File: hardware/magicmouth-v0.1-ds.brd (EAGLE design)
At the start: 100 x 80 mm, 28 parts, among them IC1 LM386N, IC2 ATMEGA168-20P, J1 1X2-3.5MM, Q1 16Mhz, U1 ARDUINOR3-NOIOREF-NOTEXT, X1 STEREOJACK

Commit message: added 5V jumper to v0.1 single sided board
added 5V jumper to v0.1 single sided board

added 5V jumper to v0.1 single sided board

added 5V jumper to v0.1 single sided board

added 5V jumper to v0.1 single sided board
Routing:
- net GND: track 211.2 -> 158.2 mm
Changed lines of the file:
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@@
 <wire x1="63.935471875" y1="42.236525" x2="63.935471875" y2="42.345471875" width="0.4064" layer="16"/>
 <wire x1="63.935471875" y1="42.345471875" x2="66.675" y2="45.085" width="0.4064" layer="16"/>
-<wire x1="27.94" y1="15.24" x2="27.94" y2="12.7" width="0.254" layer="16"/>
-<wire x1="25.4" y1="15.24" x2="27.94" y2="15.24" width="0.254" layer="16"/>
-<wire x1="24.13" y1="16.51" x2="25.4" y2="15.24" width="0.254" layer="16"/>
+<wire x1="27.94" y1="15.24" x2="27.94" y2="12.7" width="0" layer="19" extent="1-16"/>
+<wire x1="25.4" y1="15.24" x2="27.94" y2="15.24" width="0" layer="19" extent="1-16"/>
+<wire x1="24.13" y1="16.51" x2="25.4" y2="15.24" width="0" layer="19" extent="1-16"/>
 <wire x1="27.94" y1="12.7" x2="27.432" y2="12.7" width="0.254" layer="16"/>
-<wire x1="38.1" y1="59.69" x2="36.83" y2="60.96" width="0.254" layer="1"/>
-<wire x1="62.23" y1="59.69" x2="38.1" y2="59.69" width="0.254" layer="1"/>
-<wire x1="62.23" y1="40.64" x2="62.23" y2="59.69" width="0.254" layer="1"/>
+<wire x1="38.1" y1="59.69" x2="36.83" y2="60.96" width="0" layer="19" extent="1-16"/>
+<wire x1="62.23" y1="59.69" x2="38.1" y2="59.69" width="0" layer="19" extent="1-16"/>
+<wire x1="62.23" y1="40.64" x2="62.23" y2="59.69" width="0" layer="19" extent="1-16"/>
 <wire x1="36.83" y1="60.96" x2="36.576" y2="60.96" width="0.254" layer="1"/>
-<wire x1="62.23" y1="40.64" x2="61.48605" y2="39.7871" width="0.254" layer="1"/>
+<wire x1="62.23" y1="40.64" x2="61.48605" y2="39.7871" width="0" layer="19" extent="1-16"/>
 <polygon width="0" layer="16" isolate="0.4064">
 <vertex x="10.16" y="10.16"/>

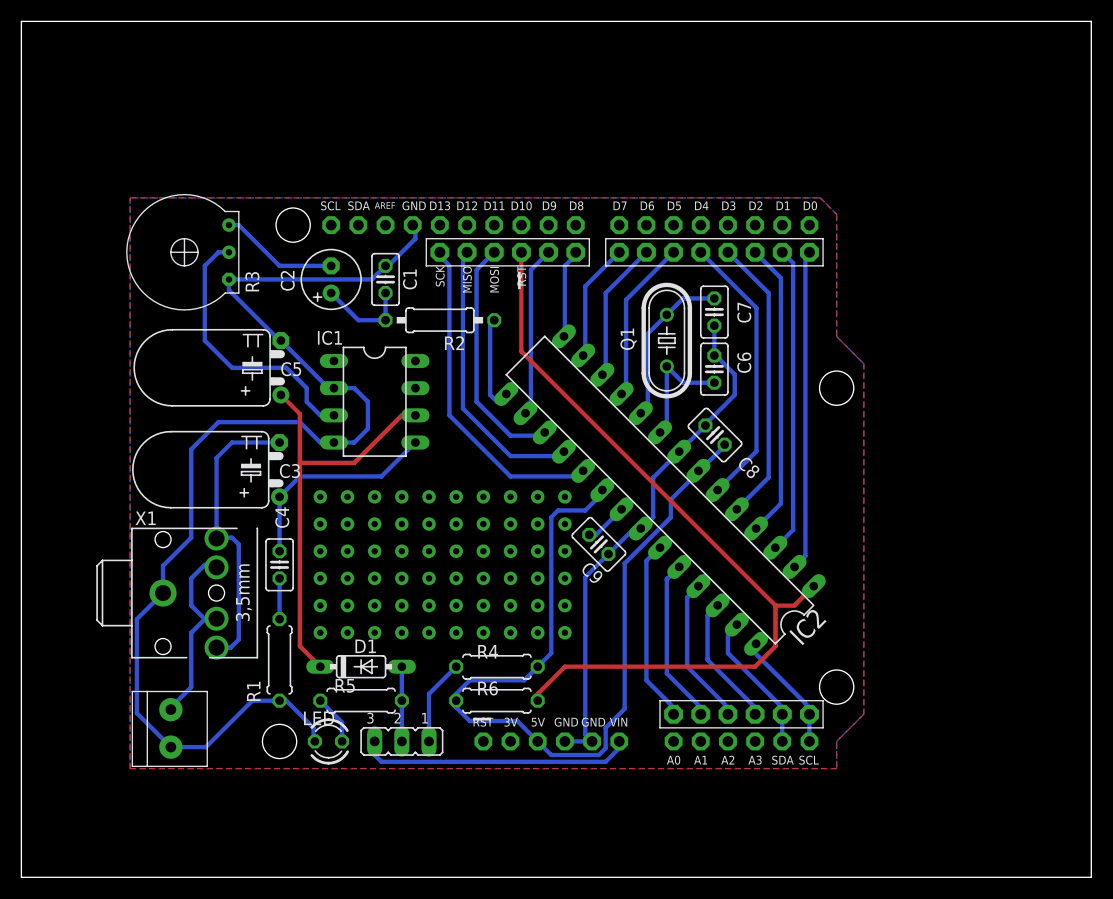
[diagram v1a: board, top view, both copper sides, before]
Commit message: added programming jumpers
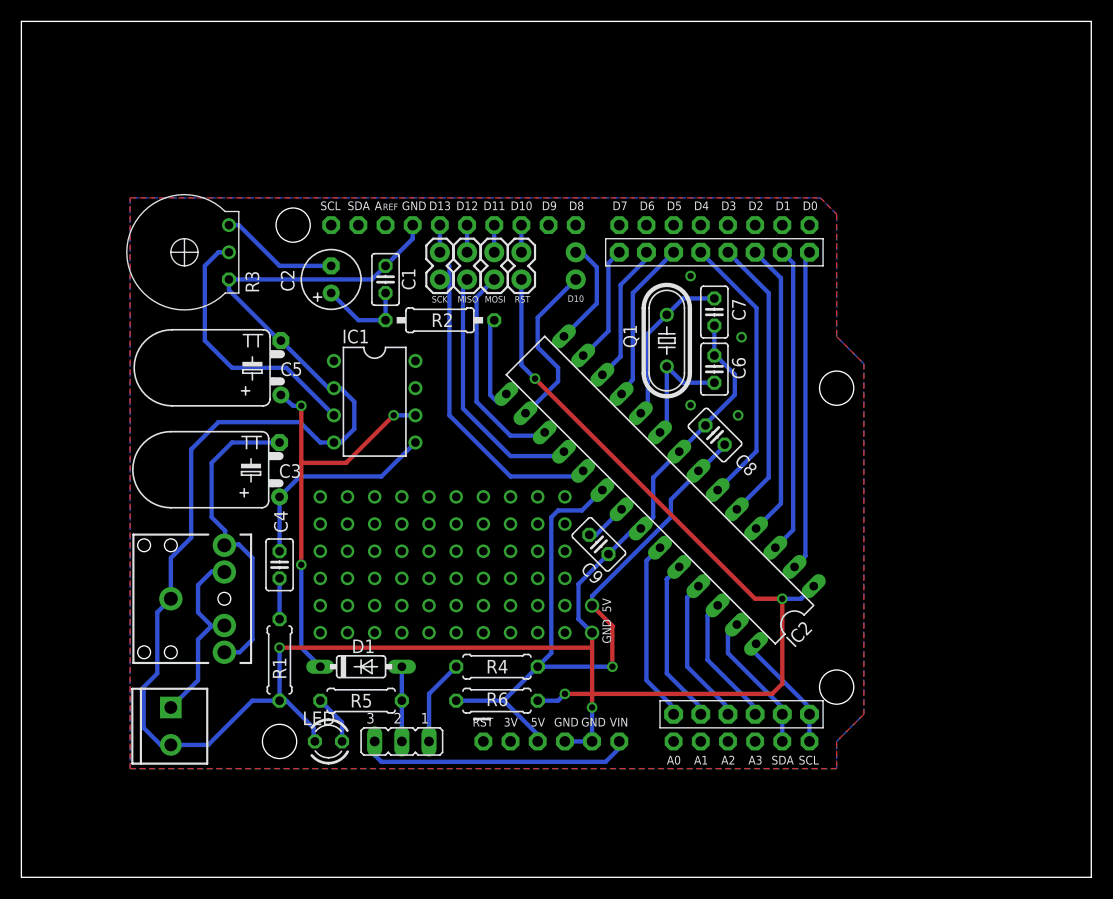
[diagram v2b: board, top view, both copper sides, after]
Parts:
- removed X1: STEREOJACK, adafruit:STX3100
- added JP5, JP6, JP7, JP8: (no value), SparkFun-Passives:1X02
- added U$2: AUDIO-JACK2PTH, SparkFun-Connectors:AUDIO-JACK
- J1: value 1X2-3.5MM -> (none); device adafruit:1X2-3.5MM -> SparkFun-Connectors:SCREWTERMINAL-3.5MM-2
- JP3: device adafruit:1X06-BIG -> SparkFun-Connectors:1X02_NO_SILK
- moved JP3 6.35 mm to (51.8, 58.4), turned to 270 degrees
- moved J1 1.90 mm to (14.0, 15.9)
- moved U$1 1.80 mm to (59.7, 22.2)
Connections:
- new net N$90: JP5.1, U1.D13
- new net N$91: JP6.1, U1.D12
- new net N$92: JP7.1, U1.D11
- new net N$93: JP8.1, U1.D10
- net +5V: now also IC2.7
- net GND: now also J1.2, U$2.SLEEVE; no longer J1.1, X1.1
- net MISO: now also JP6.2; no longer JP3.5
- net MOSI: now also JP7.2; no longer JP3.4
- net N$3: now also J1.1, U$2.RSH, U$2.TSH; no longer J1.2, X1.3, X1.4
- net N$8: now also U$2.RING, U$2.TIP; no longer X1.2, X1.5
- net SCK: now also JP5.2; no longer JP3.6
- net SS: now also JP8.2; no longer JP3.3
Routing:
- net GND: track 158.2 -> 189.0 mm, vias 0 -> 3
- net +5V: track 79.5 -> 68.0 mm, vias 0 -> 2
- net N$93: track 0.00 -> 2.54 mm
- net N$92: track 0.00 -> 2.54 mm
- net N$91: track 0.00 -> 2.54 mm
- net N$90: track 0.00 -> 2.54 mm
- net MOSI: track 22.5 -> 19.9 mm
- net MISO: track 26.2 -> 23.7 mm
- net N$24: track 8.31 -> 10.3 mm
- net SCK: track 30.7 -> 29.1 mm
- net N$8: track 27.7 -> 29.2 mm
- net N$9: track 25.5 -> 24.7 mm
- net SS: track 75.7 -> 76.3 mm, vias 0 -> 3
- net VS: track 39.6 -> 40.0 mm, vias 0 -> 3
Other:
- board text added: "A"
- board text added: "REF"
- board text removed: "AREF"

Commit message: reset switch on ss board; optional capacitor
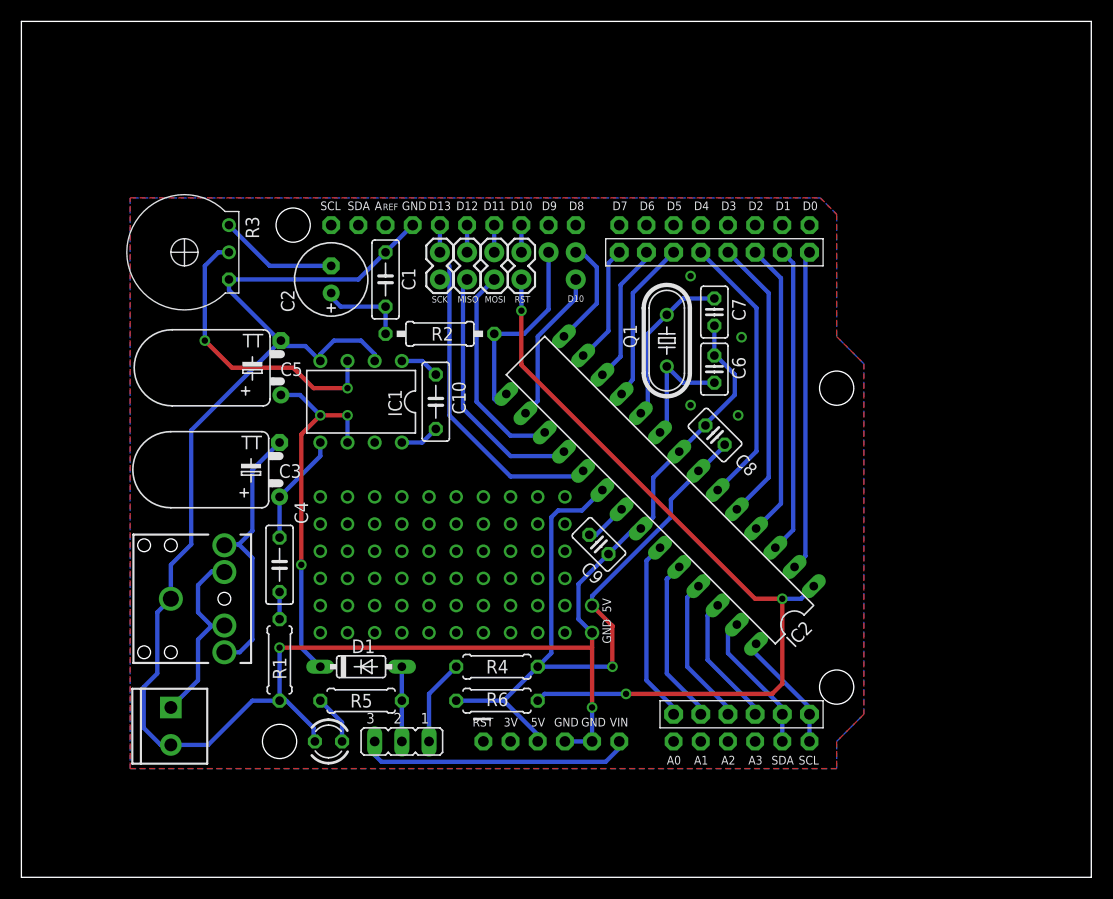
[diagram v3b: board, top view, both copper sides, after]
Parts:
- added C10: 1uF, rcl:C050-025X075
- added JP9: M01SMDNS, SparkFun-Connectors:1X01NS
- C1: device resistor:C025-025X050 -> rcl:C050-025X075
- C2: device resistor:E2,5-6 -> rcl:E2,5-7
- C4: device rcl:C025-025X050 -> rcl:C050-025X075
- moved IC1 1.27 mm to (31.8, 44.5), turned to 180 degrees
- moved R2 1.27 mm to (39.1, 50.8)
- moved U$1 0.63 mm to (59.7, 22.9)
- turned JP3 to 180 degrees
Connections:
- new net N$98: C10.1, IC1.1
- new net N$99: C10.2, IC1.8
- net N$12: now also JP9.1; no longer JP3.2
- net SIGNAL: now also JP3.2
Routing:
- net SIGNAL: track 9.21 -> 19.0 mm
- net N$1: track 19.9 -> 10.5 mm
- net VS: track 40.0 -> 34.5 mm
- net GND: track 189.0 -> 184.4 mm
- net N$8: track 29.2 -> 25.0 mm
- net N$99: track 0.00 -> 3.70 mm
- net N$98: track 0.00 -> 3.70 mm
- net N$9: track 24.7 -> 27.5 mm, vias 0 -> 2
- net N$12: track 16.1 -> 14.4 mm
- net N$4: track 3.81 -> 2.54 mm

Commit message: 220K resistor in series with gain control
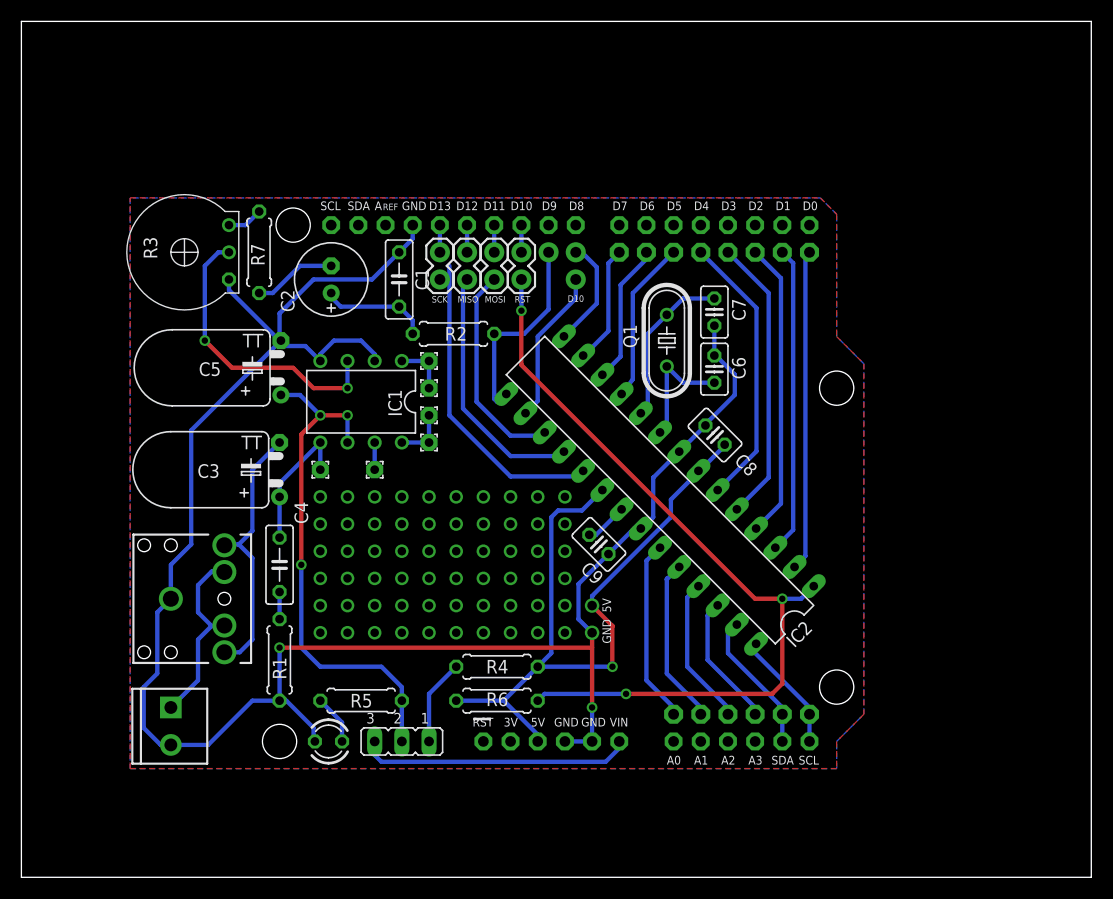
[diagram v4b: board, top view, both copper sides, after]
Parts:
- removed C10: 1uF, rcl:C050-025X075
- removed D1: 1N4148, diode:DO35-7
- added PAD1, PAD2, PAD3, PAD4, PAD5, PAD6: (no value), wirepad:1,6/0,8
- added R7: 220K, resistor:0207/7
- JP2: device adafruit:1X08-BIG -> adafruit:1X08-CLEANBIG
- JP4: device adafruit:1X06-BIG -> adafruit:1X06-CLEANBIG
- R2: device resistor:0207/10 -> rcl:0207/7
- moved R2 1.27 mm to (40.4, 50.8)
- moved C1 1.27 mm to (35.3, 55.9)
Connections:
- removed net N$27: D1.A, JP1.2, R5.2
- removed net N$98: C10.1, IC1.1
- removed net N$99: C10.2, IC1.8
- new net N$101: IC1.8, PAD3.1, PAD4.1
- new net N$58: IC1.1, PAD1.1, PAD2.1
- new net N$87: C2.-, R7.1
- new net N$94: IC1.7, PAD5.1
- net N$1: now also PAD6.1
- net N$5: now also R7.2; no longer C2.-
- net VS: now also JP1.2, R5.2; no longer D1.C
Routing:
- net VS: track 34.5 -> 48.0 mm
- net N$5: track 11.1 -> 3.35 mm
- net N$87: track 0.00 -> 7.78 mm, vias 1 -> 0
- net N$27: track 6.98 -> 0.00 mm
- net N$58: track 0.00 -> 5.08 mm, vias 1 -> 0
- net N$101: track 0.00 -> 5.08 mm
- net N$99: track 3.70 -> 0.00 mm, vias 0 -> 1
- net N$98: track 3.70 -> 0.00 mm, vias 0 -> 1
- net N$94: track 0.00 -> 2.54 mm, vias 1 -> 0
- net N$1: track 10.5 -> 13.0 mm
- net N$2: track 8.37 -> 10.2 mm

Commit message: vertical 220uF caps, 6 pin IO header
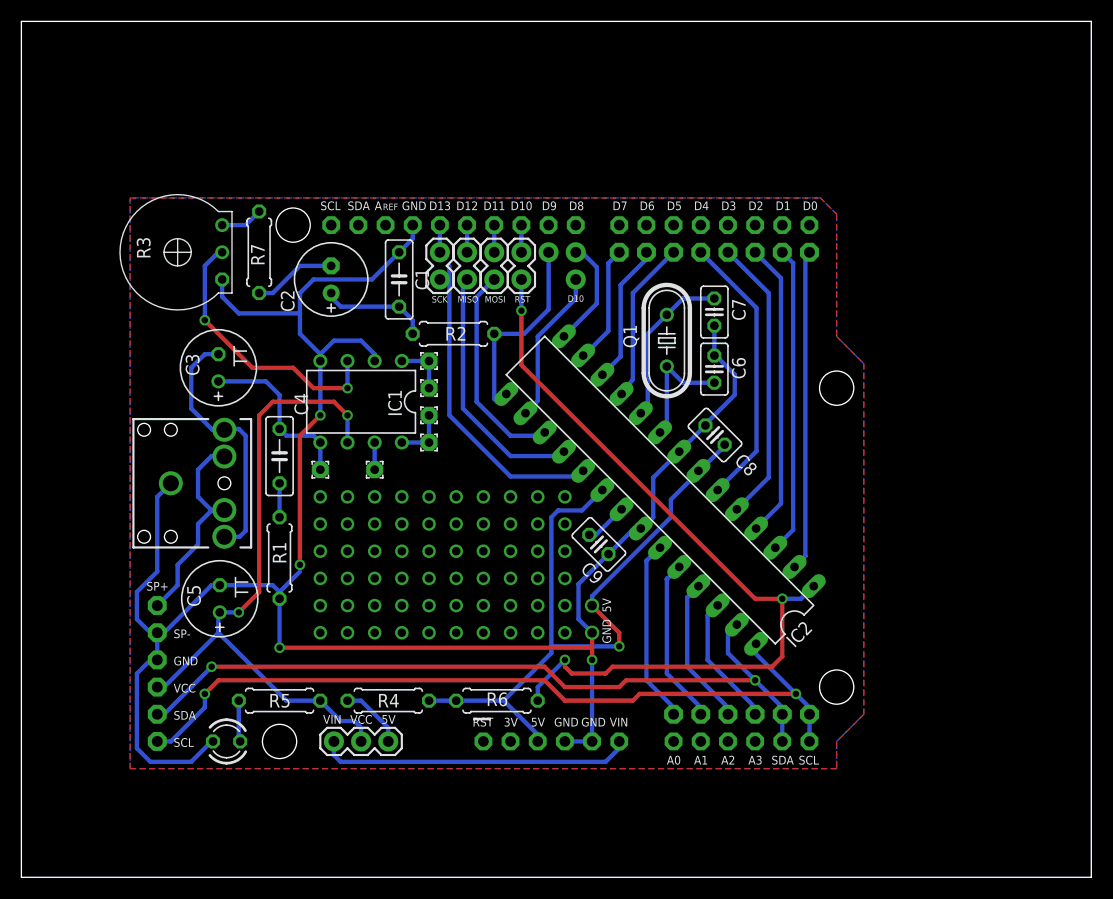
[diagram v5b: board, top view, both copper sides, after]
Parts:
- removed J1: (no value), SparkFun-Connectors:SCREWTERMINAL-3.5MM-2
- added JP10: (no value), adafruit:1X06-CLEANBIG
- C3, C5: device rcl:TT5D7L -> rcl:TT2D7
- JP1: value (none) -> JUMPER-3PTH; device jumper:JP2 -> SparkFun-Passives:1X03
- moved C5 22.3 mm to (18.5, 26.0)
- moved C3 11.1 mm to (18.4, 47.6)
- moved U$2 10.8 mm to (14.0, 36.8)
- moved R4 10.6 mm to (34.3, 16.5)
- moved C4 10.2 mm to (24.1, 39.4)
- moved LED 9.53 mm to (19.2, 12.7)
- moved R1 9.52 mm to (24.1, 29.8)
- moved R5 7.62 mm to (24.1, 16.5)
- moved JP1 1.27 mm to (34.3, 12.7)
- moved R3 0.63 mm to (14.6, 58.4)
- moved U$1 0.63 mm to (59.7, 22.2)
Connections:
- removed net N$3: J1.1, U$2.RSH, U$2.TSH
- removed net N$30: IC2.27, JP4.5, U1.A4
- removed net N$31: IC2.28, JP4.6, U1.A5
- removed net VS: C5.+, IC1.6, JP1.2, R5.2
- new net SCL: IC2.28, JP10.6, JP4.6, U1.A5
- new net SDA: IC2.27, JP10.5, JP4.5, U1.A4
- new net SP+: JP10.1, U$2.RSH, U$2.TSH
- new net VIN: JP1.3, U1.VIN
- net GND: now also JP10.2, JP10.3; no longer J1.2
- net VCC: now also C5.+, IC1.6, JP1.2, JP10.4, R5.2; no longer JP1.3, U1.VIN
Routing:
- net SCL: track 0.00 -> 75.1 mm, vias 0 -> 2
- net SDA: track 0.00 -> 72.2 mm, vias 0 -> 2
- net VS: track 48.0 -> 0.00 mm, vias 3 -> 0
- net VCC: track 25.6 -> 60.9 mm, vias 0 -> 2
- net VIN: track 0.00 -> 29.4 mm
- net SP+: track 0.00 -> 20.8 mm
- net N$3: track 17.9 -> 0.00 mm
- net N$30: track 13.4 -> 0.00 mm
- net N$31: track 11.4 -> 0.00 mm
- net GND: track 184.3 -> 193.9 mm, vias 3 -> 5
- net N$1: track 13.0 -> 16.3 mm
- net N$7: track 8.04 -> 6.13 mm
- net N$9: track 27.5 -> 25.7 mm
- net N$8: track 25.0 -> 24.2 mm
- net N$10: track 4.65 -> 3.86 mm
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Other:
- board text added: "SP+"
- board text added: "SP-"
- board text added: "VCC"

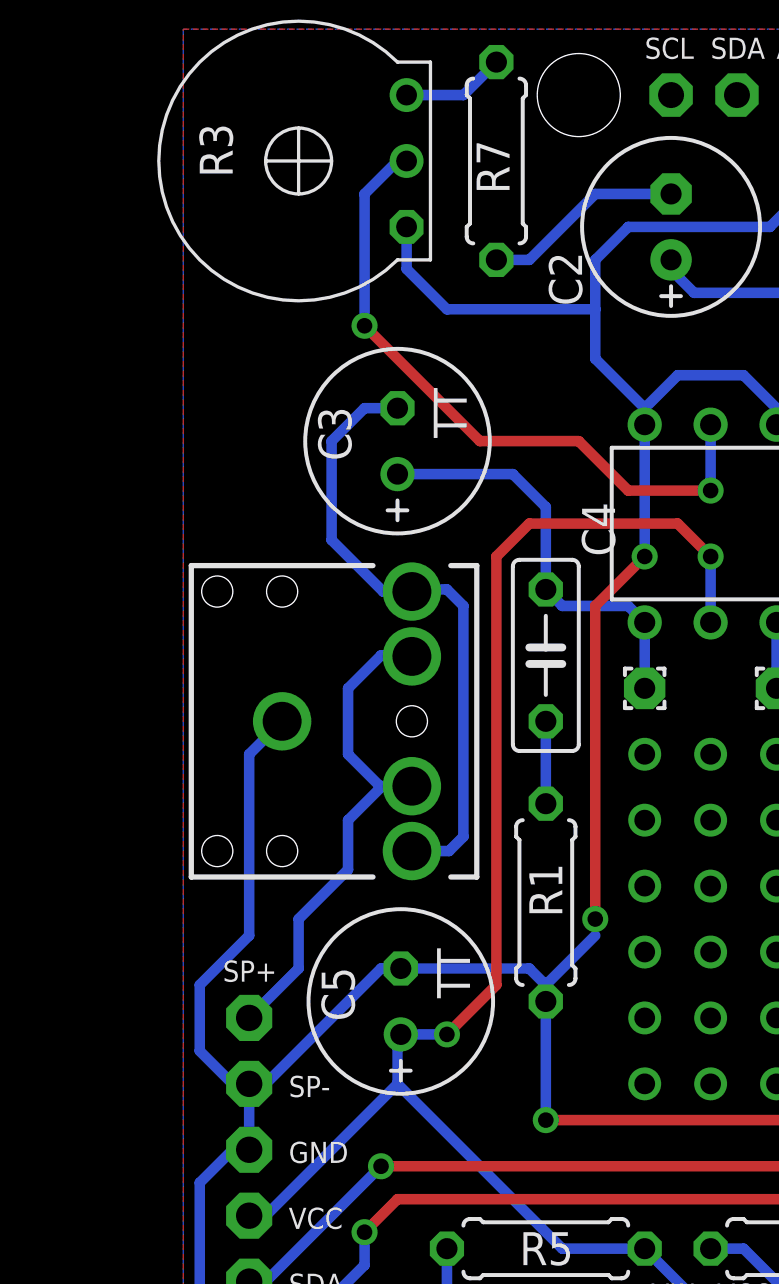
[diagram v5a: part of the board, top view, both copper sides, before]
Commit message: adjusted placement to avoid through holes directly above Arduino USB port
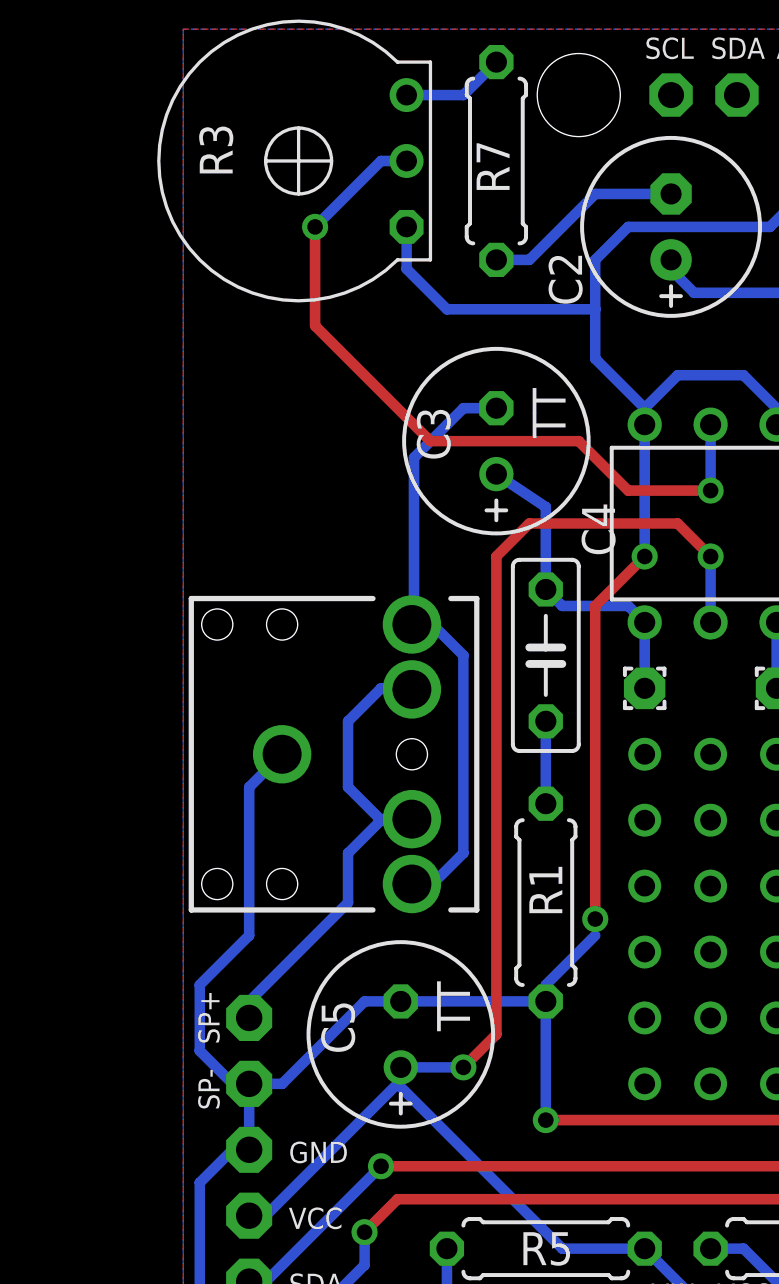
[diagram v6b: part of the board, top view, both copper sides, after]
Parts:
- moved C3 3.81 mm to (22.2, 47.6)
- moved C5 1.27 mm to (18.5, 24.8)
- moved U$2 1.27 mm to (14.0, 35.6)
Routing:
- net N$1: track 16.3 -> 12.3 mm
- net N$9: track 25.7 -> 28.8 mm
- net GND: track 193.9 -> 191.9 mm
- net SP+: track 20.8 -> 19.4 mm
- net N$8: track 24.2 -> 23.0 mm
